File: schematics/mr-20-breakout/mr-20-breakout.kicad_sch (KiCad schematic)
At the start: 6 parts, among them CN1 MR-50RMA+

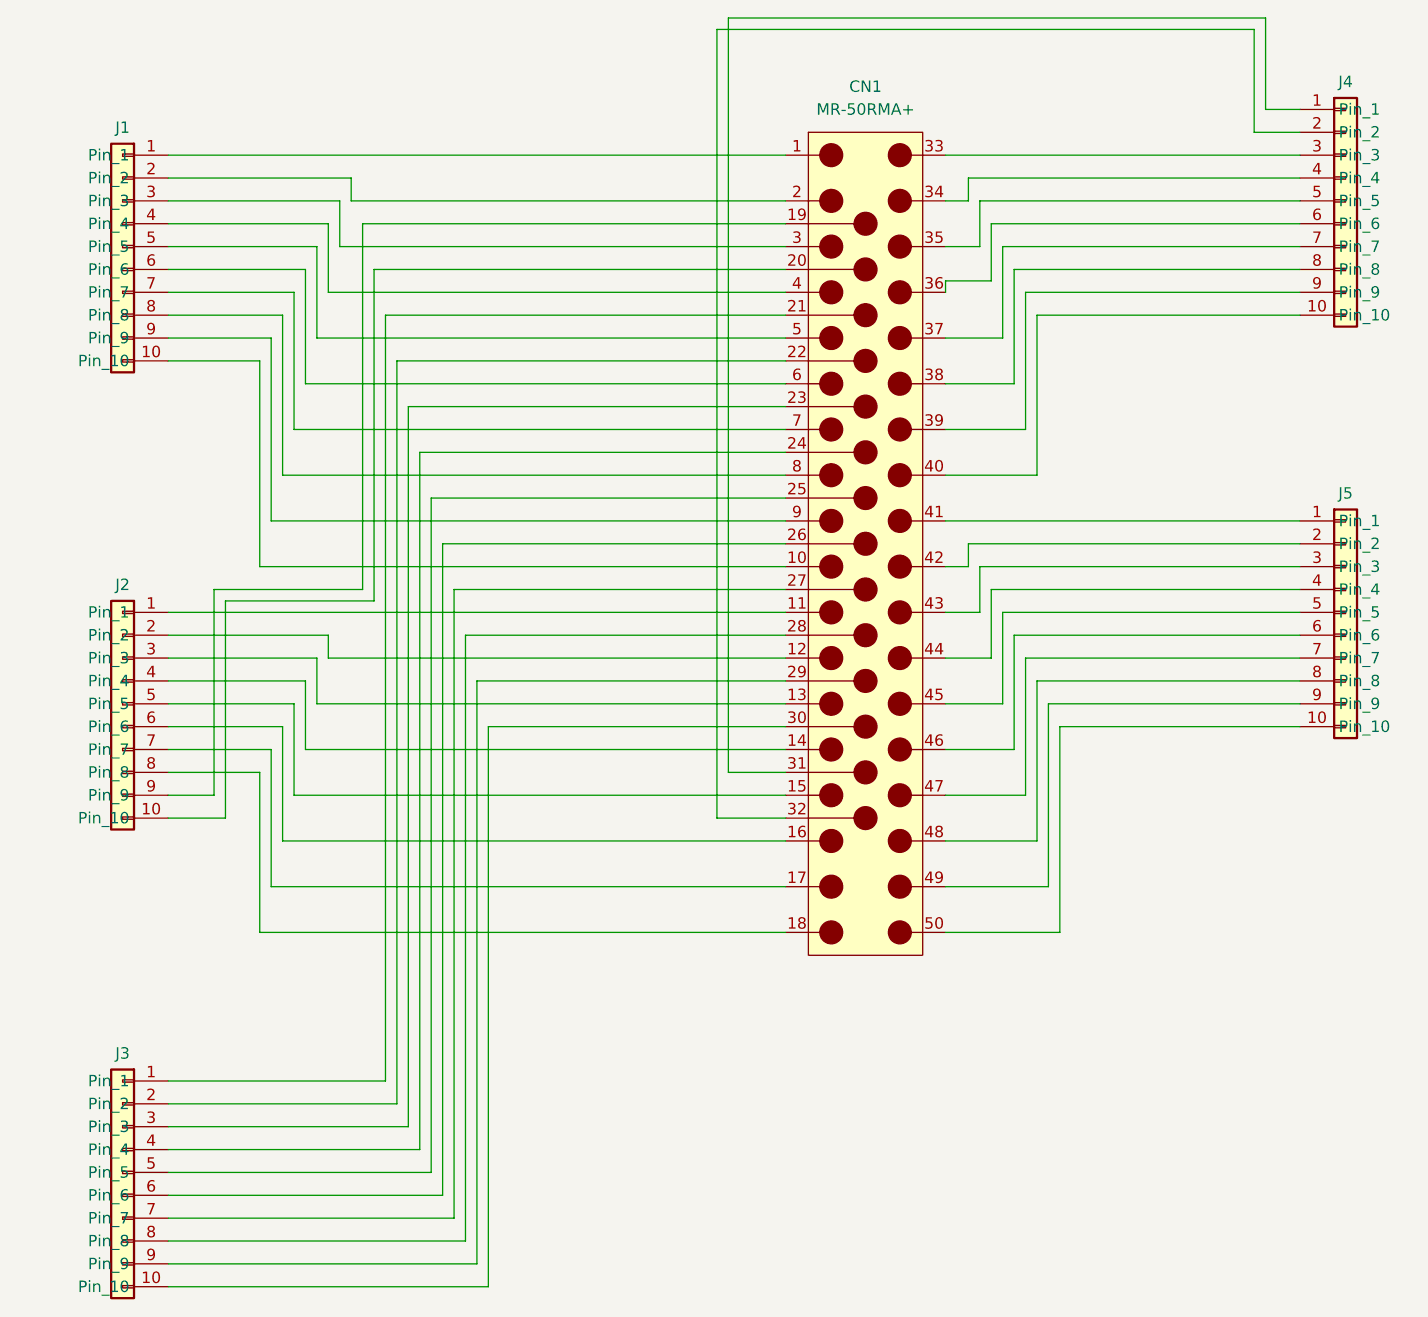
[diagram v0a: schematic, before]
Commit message: Added MR-20 breakout board schematics
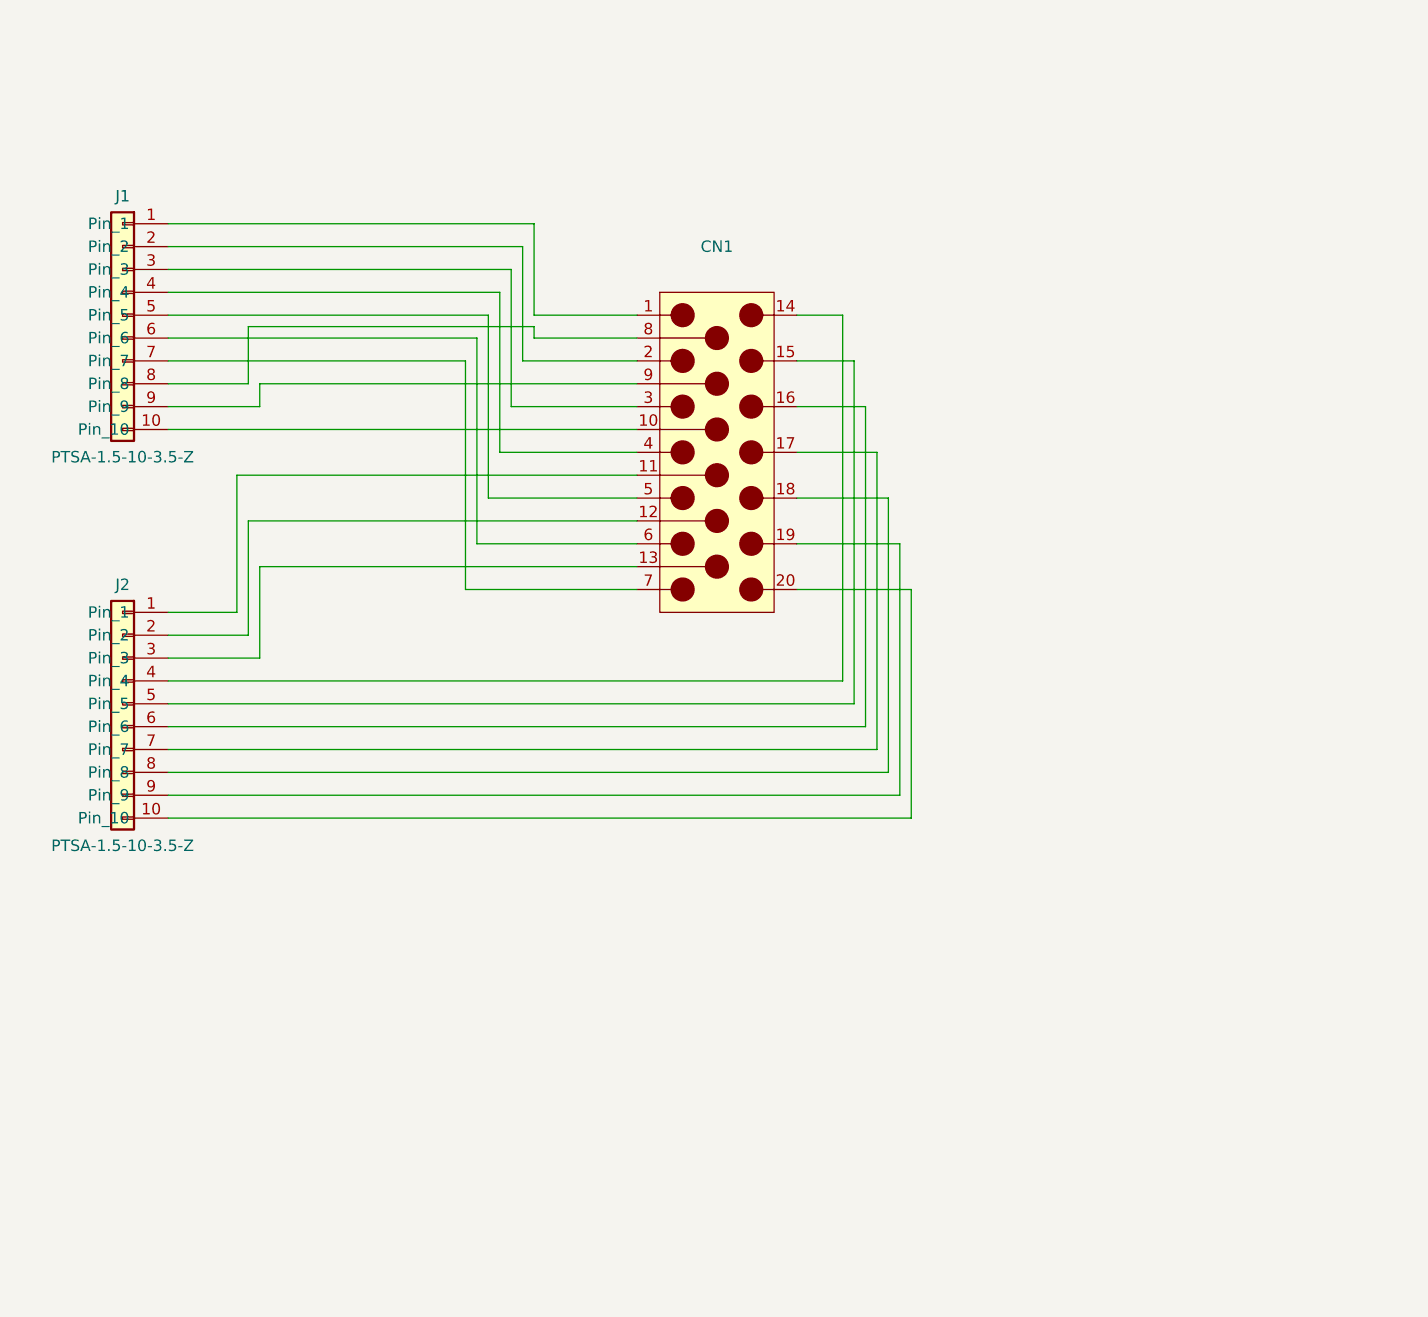
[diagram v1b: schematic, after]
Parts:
- removed CN1: MR-50RMA+, Connector_Honda:MR-50RMA+, symbol Connector_Honda:MR-50RMA+
- removed J3, J4, J5: (no value), symbol Connector_Phoenix_PTSA:PTSA-1.5-10-3.5-Z
- added CN1: (no value), symbol Connector_Honda:MR-20RMA+
- J1, J2: value (none) -> PTSA-1.5-10-3.5-Z; footprint (none) -> Connector_Phoenix_PTSA:PhoenixContact_PTSA_1,5_10_3,5-Z
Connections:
- net at J2.1 (Pin_1): now also CN1.11
- net at J2.10 (Pin_10): now also CN1.20
- net at J2.2 (Pin_2): now also CN1.12
- net at J2.3 (Pin_3): now also CN1.13
- net at J2.4 (Pin_4): now also CN1.14
- net at J2.5 (Pin_5): now also CN1.15
- net at J2.6 (Pin_6): now also CN1.16
- net at J2.7 (Pin_7): now also CN1.17
- net at J2.8 (Pin_8): now also CN1.18
- net at J2.9 (Pin_9): now also CN1.19
- net at J1.1 (Pin_1): now also CN1.1
- net at J1.10 (Pin_10): now also CN1.10
- net at J1.2 (Pin_2): now also CN1.2
- net at J1.3 (Pin_3): now also CN1.3
- net at J1.4 (Pin_4): now also CN1.4
- net at J1.5 (Pin_5): now also CN1.5
- net at J1.6 (Pin_6): now also CN1.6
- net at J1.7 (Pin_7): now also CN1.7
- net at J1.8 (Pin_8): now also CN1.8
- net at J1.9 (Pin_9): now also CN1.9
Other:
- title: MR-50 Breakout Board -> MR-20 Breakout Board
- moved on the sheet: J1
